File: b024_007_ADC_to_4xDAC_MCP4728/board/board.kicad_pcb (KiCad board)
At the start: 2 copper layers, 21 x 13 mm, 14 parts, among them J1 007_ADC_2x5, J2 001_I2C_2x5, U1 MCP4728

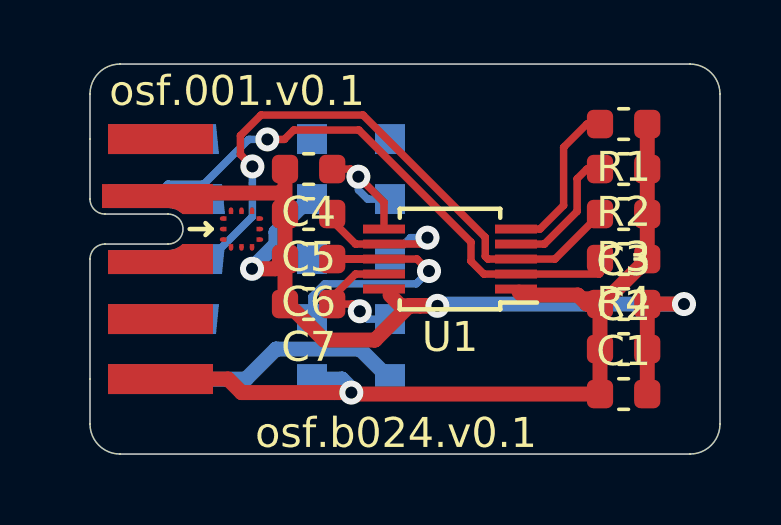
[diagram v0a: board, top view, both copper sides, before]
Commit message: updated connectors
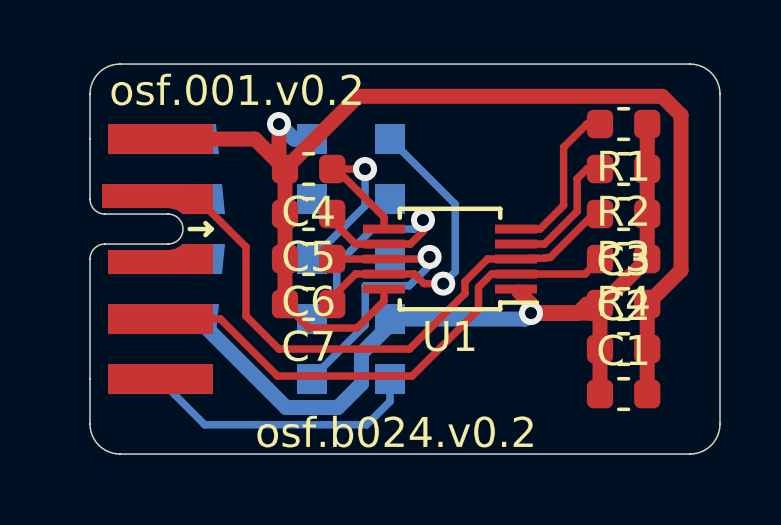
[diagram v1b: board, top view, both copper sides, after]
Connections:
- J2 pad 2: (no net) -> Net-(J2-Pad2)
- J2 pad 3: Net-(J2-Pad3) -> (no net)
- R3 pad 2: Net-(J2-Pad4) -> Net-(J2-Pad2)
- R4 pad 2: Net-(J2-Pad3) -> Net-(J2-Pad4)
- U1 pad 2: Net-(J2-Pad3) -> Net-(J2-Pad4)
- U1 pad 3: Net-(J2-Pad4) -> Net-(J2-Pad2)
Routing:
- net Net-(J2-Pad3): track 18.7 -> 0.00 mm, vias 1 -> 0
- net Net-(J2-Pad2): track 0.00 -> 18.5 mm
- net GND: track 33.0 -> 40.6 mm, vias 3 -> 1
- net Net-(C7-Pad1): track 4.40 -> 10.3 mm
- net Net-(J2-Pad4): track 22.0 -> 17.5 mm, vias 1 -> 0
- net Net-(C5-Pad1): track 5.37 -> 9.77 mm
- net Net-(C4-Pad1): track 4.70 -> 7.61 mm
- net VCC: track 32.0 -> 33.5 mm
- net Net-(J1-Pad10): track 8.53 -> 9.40 mm
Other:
- board text added: "osf.001.v0.2"
- board text added: "osf.b024.v0.2"
- board text removed: "osf.001.v0.1"
- board text removed: "osf.b024.v0.1"
